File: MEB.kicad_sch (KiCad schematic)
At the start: 4 parts

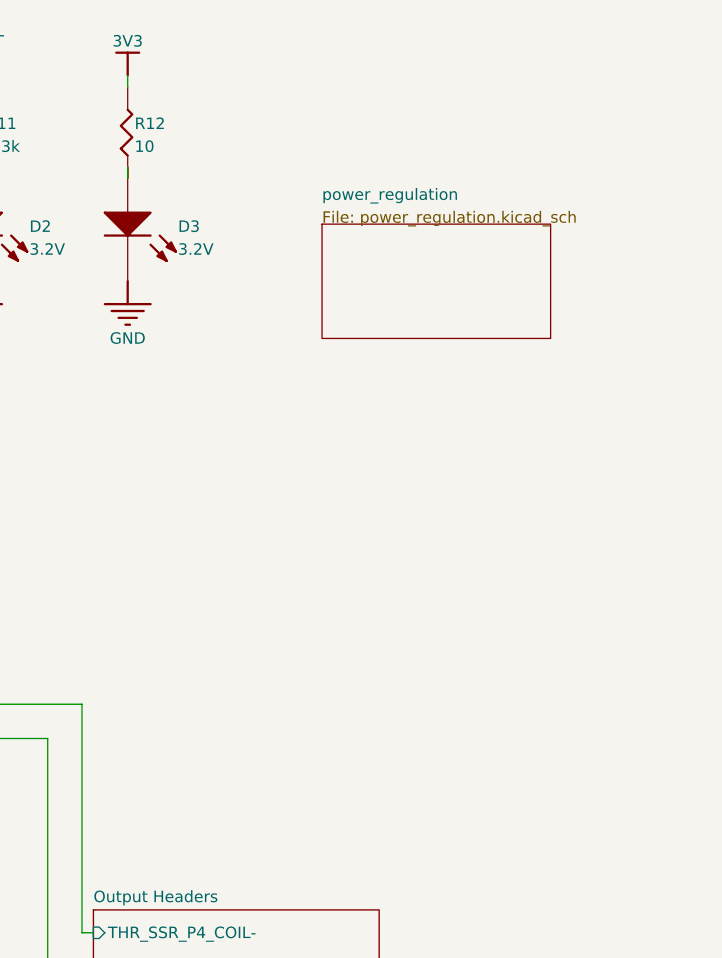
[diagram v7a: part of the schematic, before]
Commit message: Finalized schematic and began assigning footprints
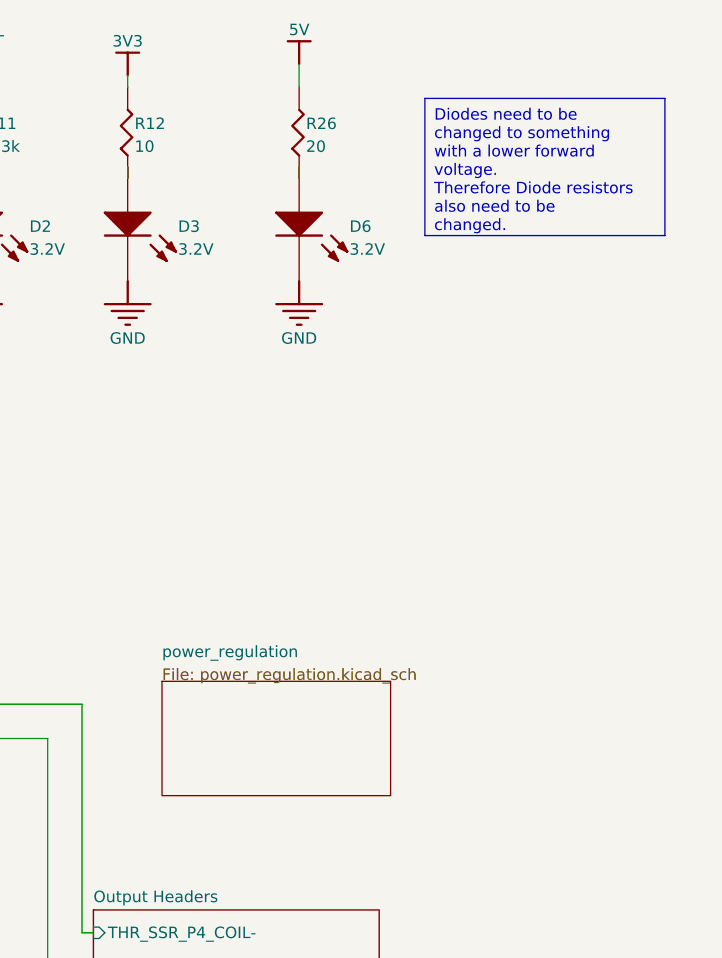
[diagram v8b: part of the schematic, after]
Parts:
- added D6: 3.2V, AltiumImport:0805_A, symbol MEB-altium-import:root_3_WE-LED_K1A2-2
- added R26: 20, Resistor_SMD:R_0805_2012Metric_Pad1.20x1.40mm_HandSolder, symbol MEB-altium-import:root_1_ERJ-6ENF10R0V
- R11, R12: footprint AltiumImport:SMD-0805-RES -> Resistor_SMD:R_0805_2012Metric_Pad1.20x1.40mm_HandSolder
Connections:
- net GND: now also D6.1 (K)
- new net: D6.2 (A), R26.1
- new net 5V: R26.2
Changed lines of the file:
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@@
     (stroke (width 0) (type default))
+  )
+  (wire (pts (xy 226.06 72.39) (xy 226.06 71.12))
+    (stroke (width 0.254) (type default))
   )
   (wire (pts (xy 162.56 130.81) (xy 201.93 130.81))
@@
   (wire (pts (xy 55.88 172.72) (xy 67.31 172.72))
     (stroke (width 0) (type default))
+  )
+  (wire (pts (xy 226.06 59.69) (xy 226.06 62.23))
+    (stroke (width 0.254) (type default))
   )
   (image (at 65.4735 68.722) (scale 1.20291)
@@
     )
   )
+  (text_box "Diodes need to be changed to something with a lower forward voltage.\nTherefore Diode resistors also need to be changed.\n"
+    (at 240.03 63.5 0) (size 26.67 15.24)
+    (stroke (width 0) (type default))
+    (fill (type none))
+    (effects (font (size 1.27 1.27)) (justify left top))
+  )
   (text_box "MEBv1:\n - D1-D3: 10mA x 3 = 30mA\nsystem_SSR_control:\n - insignificant\npower_regulation: \n - 15mA @ 60% efficiency (estimated)\nMSP430: \n - MSP430 Launchpad: 5mA (estimated)\nTOTAL = 50mA (estimated)"
     (at 179.07 63.5 0) (size -39.37 25.4)
@@
       (effects (font (size 1.27 1.27)) (justify left bottom))
     )
-    (property "Footprint" "AltiumImport:SMD-0805-RES" (at 207.01 67.31 0)
+    (property "Footprint" "Resistor_SMD:R_0805_2012Metric_Pad1.20x1.40mm_HandSolder" (at 207.01 67.31 0)
       (effects (font (size 1.27 1.27)) hide)
     )
@@
     )
   )
+  (symbol (lib_id "MEB-altium-import:5V") (at 226.06 59.69 180) (unit 1)
+    (in_bom yes) (on_board yes) (dnp no)
+    (property "Reference" "#PWR028" (at 224.79 53.34 0)
+      (effects (font (size 1.27 1.27)) hide)
+    )
+    (property "Value" "5V" (at 226.06 55.88 0)
+      (effects (font (size 1.27 1.27)))
+    )
+    (property "Footprint" "" (at 226.06 59.69 0)
+      (effects (font (size 1.27 1.27)) hide)
+    )
+    (property "Datasheet" "" (at 226.06 59.69 0)
+      (effects (font (size 1.27 1.27)) hide)
+    )
+    (pin "")
+    (instances
+      (project "MEB"
+        (path "/228e4997-23c1-4c21-939b-583cad26a5e3"
+          (reference "#PWR028") (unit 1)
+        )
+      )
+    )
+  )
   (symbol (lib_id "MEB-altium-import:GND") (at 190.5 83.82 0) (unit 1)
     (in_bom yes) (on_board yes) (dnp no)
@@
         (path "/228e4997-23c1-4c21-939b-583cad26a5e3"
           (reference "#PWR0103") (unit 1)
+        )
+      )
+    )
+  )
+  (symbol (lib_id "MEB-altium-import:root_3_WE-LED_K1A2-2") (at 226.06 76.2 0) (unit 1)
+    (in_bom yes) (on_board yes) (dnp no)
+    (property "Reference" "D6" (at 231.648 78.486 0)
+      (effects (font (size 1.27 1.27)) (justify left bottom))
+    )
+    (property "Value" "3.2V" (at 231.648 81.026 0)
+      (effects (font (size 1.27 1.27)) (justify left bottom))
+    )
+    (property "Footprint" "AltiumImport:0805_A" (at 226.06 76.2 0)
+      (effects (font (size 1.27 1.27)) hide)
+    )
+    (property "Datasheet" "" (at 226.06 76.2 0)
+      (effects (font (size 1.27 1.27)) hide)
+    )
+    (property "Part Number" "150080GS75000" (at 226.06 76.2 0)
+      (effects (font (size 1.27 1.27)) hide)
+    )
+    (pin "1")
+    (pin "2")
+    (instances
+      (project "MEB"
+        (path "/228e4997-23c1-4c21-939b-583cad26a5e3"
+          (reference "D6") (unit 1)
         )
       )
@@
     )
   )
+  (symbol (lib_id "MEB-altium-import:GND") (at 226.06 83.82 0) (unit 1)
+    (in_bom yes) (on_board yes) (dnp no)
+    (property "Reference" "#PWR029" (at 226.06 83.82 0)
+      (effects (font (size 1.27 1.27)) hide)
+    )
+    (property "Value" "GND" (at 226.06 90.17 0)
+      (effects (font (size 1.27 1.27)))
+    )
+    (property "Footprint" "" (at 226.06 83.82 0)
+      (effects (font (size 1.27 1.27)) hide)
+    )
+    (property "Datasheet" "" (at 226.06 83.82 0)
+      (effects (font (size 1.27 1.27)) hide)
+    )
+    (pin "")
+    (instances
+      (project "MEB"
+        (path "/228e4997-23c1-4c21-939b-583cad26a5e3"
+          (reference "#PWR029") (unit 1)
+        )
+      )
+    )
+  )
   (symbol (lib_id "MEB-altium-import:root_1_ERJ-6GEYJ132V") (at 190.5 67.31 0) (unit 1)
     (in_bom yes) (on_board yes) (dnp no)
@@
       (effects (font (size 1.27 1.27)) (justify left bottom))
     )
-    (property "Footprint" "AltiumImport:SMD-0805-RES" (at 190.5 67.31 0)
+    (property "Footprint" "Resistor_SMD:R_0805_2012Metric_Pad1.20x1.40mm_HandSolder" (at 190.5 67.31 0)
       (effects (font (size 1.27 1.27)) hide)
     )
@@
     )
   )
+  (symbol (lib_id "MEB-altium-import:root_1_ERJ-6ENF10R0V") (at 226.06 67.31 0) (unit 1)
+    (in_bom yes) (on_board yes) (dnp no)
+    (property "Reference" "R26" (at 226.822 67.056 0)
+      (effects (font (size 1.27 1.27)) (justify left bottom))
+    )
+    (property "Value" "20" (at 226.822 69.596 0)
+      (effects (font (size 1.27 1.27)) (justify left bottom))
+    )
+    (property "Footprint" "Resistor_SMD:R_0805_2012Metric_Pad1.20x1.40mm_HandSolder" (at 226.06 67.31 0)
+      (effects (font (size 1.27 1.27)) hide)
+    )
+    (property "Datasheet" "" (at 226.06 67.31 0)
+      (effects (font (size 1.27 1.27)) hide)
+    )
+    (property "Part Number" "RC0805FR-0710RL" (at 226.06 67.31 0)
+      (effects (font (size 1.27 1.27)) hide)
+    )
+    (pin "1")
+    (pin "2")
+    (instances
+      (project "MEB"
+        (path "/228e4997-23c1-4c21-939b-583cad26a5e3"
+          (reference "R26") (unit 1)
+        )
+      )
+    )
+  )
   (sheet (at 83.82 153.67) (size 22.86 7.62) (fields_autoplaced)
     (stroke (width 0) (type solid) (color 128 0 0 1))
@@
     )
   )
-  (sheet (at 228.6 77.47) (size 25.4 12.7) (fields_autoplaced)
+  (sheet (at 210.82 128.27) (size 25.4 12.7) (fields_autoplaced)
     (stroke (width 0) (type solid) (color 128 0 0 1))
     (fill (color 109 158 235 1.0000))
-    (property "Sheetname" "power_regulation" (at 228.6 74.93 0)
+    (property "Sheetname" "power_regulation" (at 210.82 125.73 0)
       (effects (font (size 1.27 1.27)) (justify left bottom))
     )
-    (property "Sheetfile" "power_regulation.kicad_sch" (at 228.6 77.47 0)
+    (property "Sheetfile" "power_regulation.kicad_sch" (at 210.82 128.27 0)
       (effects (font (size 1.27 1.27)) (justify left bottom))
     )
